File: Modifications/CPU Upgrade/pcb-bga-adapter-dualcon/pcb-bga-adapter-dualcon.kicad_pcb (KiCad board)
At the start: 2 copper layers, 23 x 23 mm, 3 parts, among them J1 54722-0604, J2 55560-0607

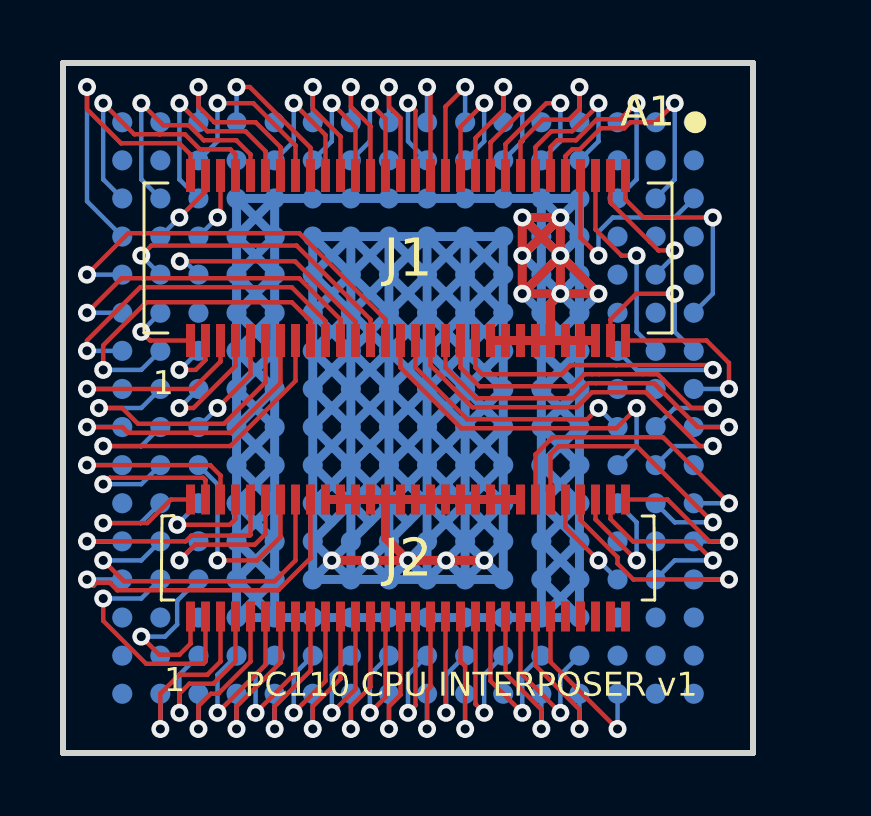
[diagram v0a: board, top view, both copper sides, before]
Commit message: Updated CPU Board
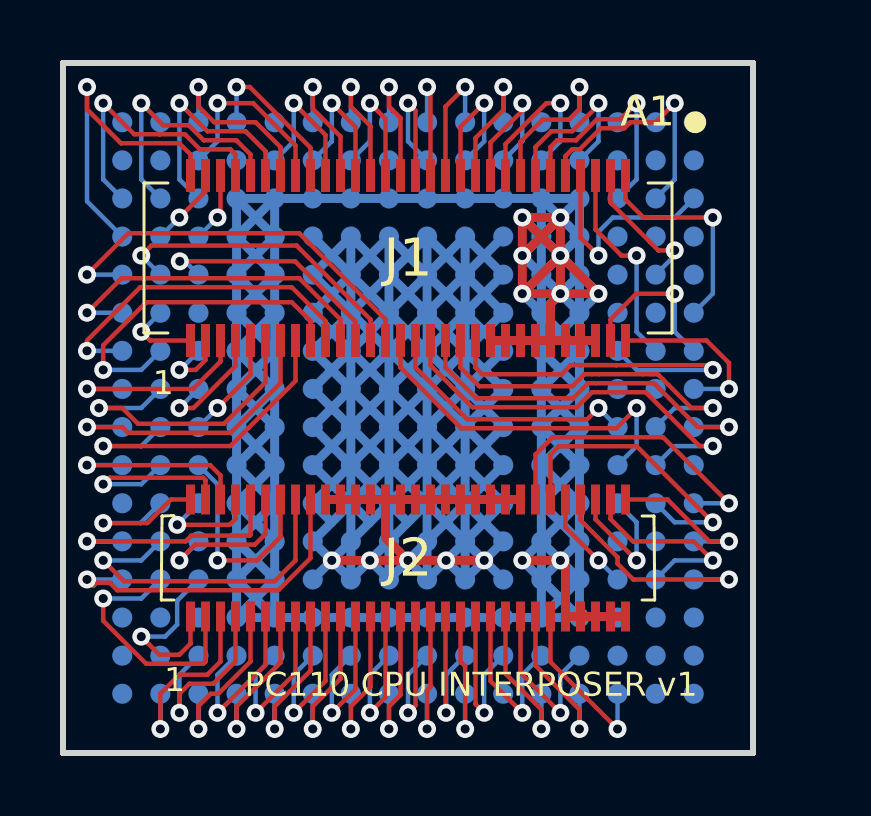
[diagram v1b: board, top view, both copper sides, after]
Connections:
- J2 pad 51: unconnected-(J2-Pad51) -> VCC
- J2 pad 53: unconnected-(J2-Pad53) -> VCC
- J2 pad 55: unconnected-(J2-Pad55) -> VCC
- J2 pad 57: unconnected-(J2-Pad57) -> VCC
- J2 pad 59: unconnected-(J2-Pad59) -> VCC
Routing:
- net GND: track 251.5 -> 215.9 mm
- net VCC: track 185.3 -> 192.3 mm, vias 7 -> 9
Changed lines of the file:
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@@
 	(net 137 "D23")
 	(net 138 "VCC")
-	(net 139 "unconnected-(J2-Pad51)")
-	(net 140 "unconnected-(J2-Pad59)")
-	(net 141 "unconnected-(J2-Pad53)")
-	(net 142 "unconnected-(J2-Pad55)")
-	(net 143 "unconnected-(J2-Pad57)")
 	(footprint "pcb-bga-library:555600607"
 		(layer "F.Cu")
@@
 			(size 0.3 1)
 			(layers "F.Cu" "F.Mask" "F.Paste")
-			(net 139 "unconnected-(J2-Pad51)")
+			(net 138 "VCC")
 			(pinfunction "51")
 			(pintype "passive")
@@
 			(size 0.3 1)
 			(layers "F.Cu" "F.Mask" "F.Paste")
-			(net 141 "unconnected-(J2-Pad53)")
+			(net 138 "VCC")
 			(pinfunction "53")
 			(pintype "passive")
@@
 			(size 0.3 1)
 			(layers "F.Cu" "F.Mask" "F.Paste")
-			(net 142 "unconnected-(J2-Pad55)")
+			(net 138 "VCC")
 			(pinfunction "55")
 			(pintype "passive")
@@
 			(size 0.3 1)
 			(layers "F.Cu" "F.Mask" "F.Paste")
-			(net 143 "unconnected-(J2-Pad57)")
+			(net 138 "VCC")
 			(pinfunction "57")
 			(pintype "passive")
@@
 			(size 0.3 1)
 			(layers "F.Cu" "F.Mask" "F.Paste")
-			(net 140 "unconnected-(J2-Pad59)")
+			(net 138 "VCC")
 			(pinfunction "59")
 			(pintype "passive")
@@
 	)
 	(segment
-		(start 108.325 105.785)
-		(end 108.325 117.215)
-		(width 0.3)
-		(layer "B.Cu")
-		(net 42)
-	)
-	(segment
-		(start 108.325 117.215)
-		(end 114.675 117.215)
-		(width 0.3)
-		(layer "B.Cu")
-		(net 42)
-	)
-	(segment
 		(start 110.23 115.31)
 		(end 108.325 113.405)
@@
 	)
 	(segment
-		(start 114.675 105.785)
-		(end 108.325 105.785)
-		(width 0.3)
-		(layer "B.Cu")
-		(net 42)
-	)
-	(segment
 		(start 109.595 117.215)
 		(end 114.675 112.135)
@@
 	)
 	(segment
-		(start 114.675 117.215)
-		(end 114.675 105.785)
-		(width 0.3)
-		(layer "B.Cu")
-		(net 42)
-	)
-	(segment
 		(start 112.135 105.785)
 		(end 112.135 117.215)
@@
 	)
 	(segment
+		(start 115.31 116.58)
+		(end 116.58 116.58)
+		(width 0.3)
+		(layer "F.Cu")
+		(net 138)
+	)
+	(segment
+		(start 116.58 116.58)
+		(end 116.75 116.75)
+		(width 0.3)
+		(layer "F.Cu")
+		(net 138)
+	)
+	(segment
 		(start 116.58 107.69)
 		(end 116.25 108.02)
@@
 	)
 	(segment
+		(start 116.75 118.45)
+		(end 118.75 118.45)
+		(width 0.3)
+		(layer "F.Cu")
+		(net 138)
+	)
+	(segment
 		(start 115.31 107.69)
 		(end 116.58 106.42)
@@
 	)
 	(segment
+		(start 116.75 116.75)
+		(end 116.75 118.45)
+		(width 0.3)
+		(layer "F.Cu")
+		(net 138)
+	)
+	(segment
 		(start 116.58 105.15)
 		(end 116.58 107.69)
@@
 	)
 	(via
+		(at 116.58 116.58)
+		(size 0.6)
+		(drill 0.3)
+		(layers "F.Cu" "B.Cu")
+		(net 138)
+	)
+	(via
 		(at 116.58 105.15)
 		(size 0.6)
@@
 		(net 138)
 	)
+	(via
+		(at 115.31 116.58)
+		(size 0.6)
+		(drill 0.3)
+		(layers "F.Cu" "B.Cu")
+		(net 138)
+	)
 	(segment
 		(start 107.055 105.785)
@@
 	)
 	(segment
-		(start 117.215 117.215)
-		(end 115.945 115.945)
-		(width 0.3)
-		(layer "B.Cu")
-		(net 138)
-	)
-	(segment
 		(start 107.055 107.055)
 		(end 105.785 105.785)
@@
 	)
 	(segment
+		(start 117.215 117.215)
+		(end 116.58 116.58)
+		(width 0.3)
+		(layer "B.Cu")
+		(net 138)
+	)
+	(segment
 		(start 117.215 105.785)
 		(end 116.58 106.42)
@@
 	)
 	(segment
+		(start 115.31 116.58)
+		(end 115.945 117.215)
+		(width 0.3)
+		(layer "B.Cu")
+		(net 138)
+	)
+	(segment
 		(start 115.945 104.515)
 		(end 116.58 105.15)
@@
 	(segment
 		(start 117.215 115.945)
-		(end 115.945 117.215)
+		(end 116.58 116.58)
 		(width 0.3)
 		(layer "B.Cu")
@@
 	)
 	(segment
+		(start 116.58 116.58)
+		(end 115.945 115.945)
+		(width 0.3)
+		(layer "B.Cu")
+		(net 138)
+	)
+	(segment
 		(start 117.215 113.405)
 		(end 115.945 114.675)
@@
 		(width 0.3)
 		(layer "B.Cu")
+		(net 138)
+	)
+	(segment
+		(start 116.58 116.58)
+		(end 115.945 117.215)
+		(width 0.3)
+		(layer "B.Cu")
+		(net 138)
+	)
+	(segment
+		(start 115.31 116.58)
+		(end 115.945 115.945)
+		(width 0.3)
+		(layer "B.Cu")
